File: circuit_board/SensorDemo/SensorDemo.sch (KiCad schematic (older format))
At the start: 47 parts, among them K1 PB, P1 CONN3X2, P2 CONN3X2, U1 TLV1117-33CDCYR, U2 dsPIC33EP32GP502, U3 LTC1658, U4 INA126, U5 REF1925, U6 REF1925, X1 CRYSTAL

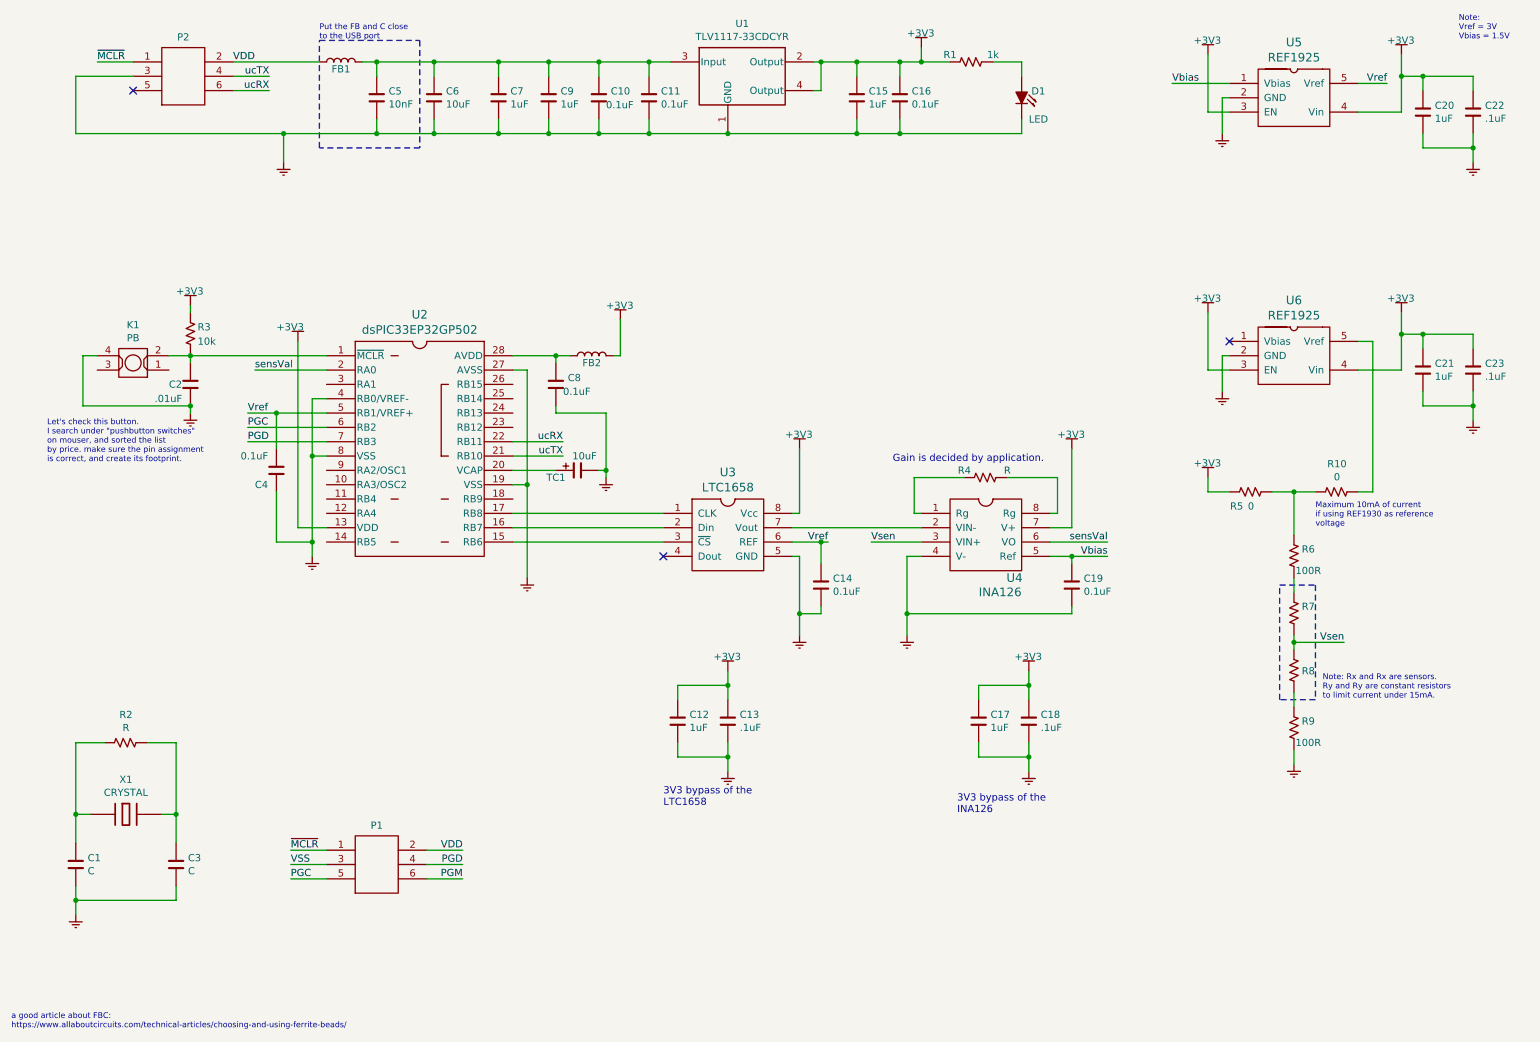
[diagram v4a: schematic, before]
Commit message: symbol and pcb footprint updated
Added test points to replace the sensors.
TC2030 part modified.
the button needs modification.
TG connector:
https://www.tag-connect.com/product/tc2030-alt-nl-no-legs-cable-for-use-with-altera-usb-blaster
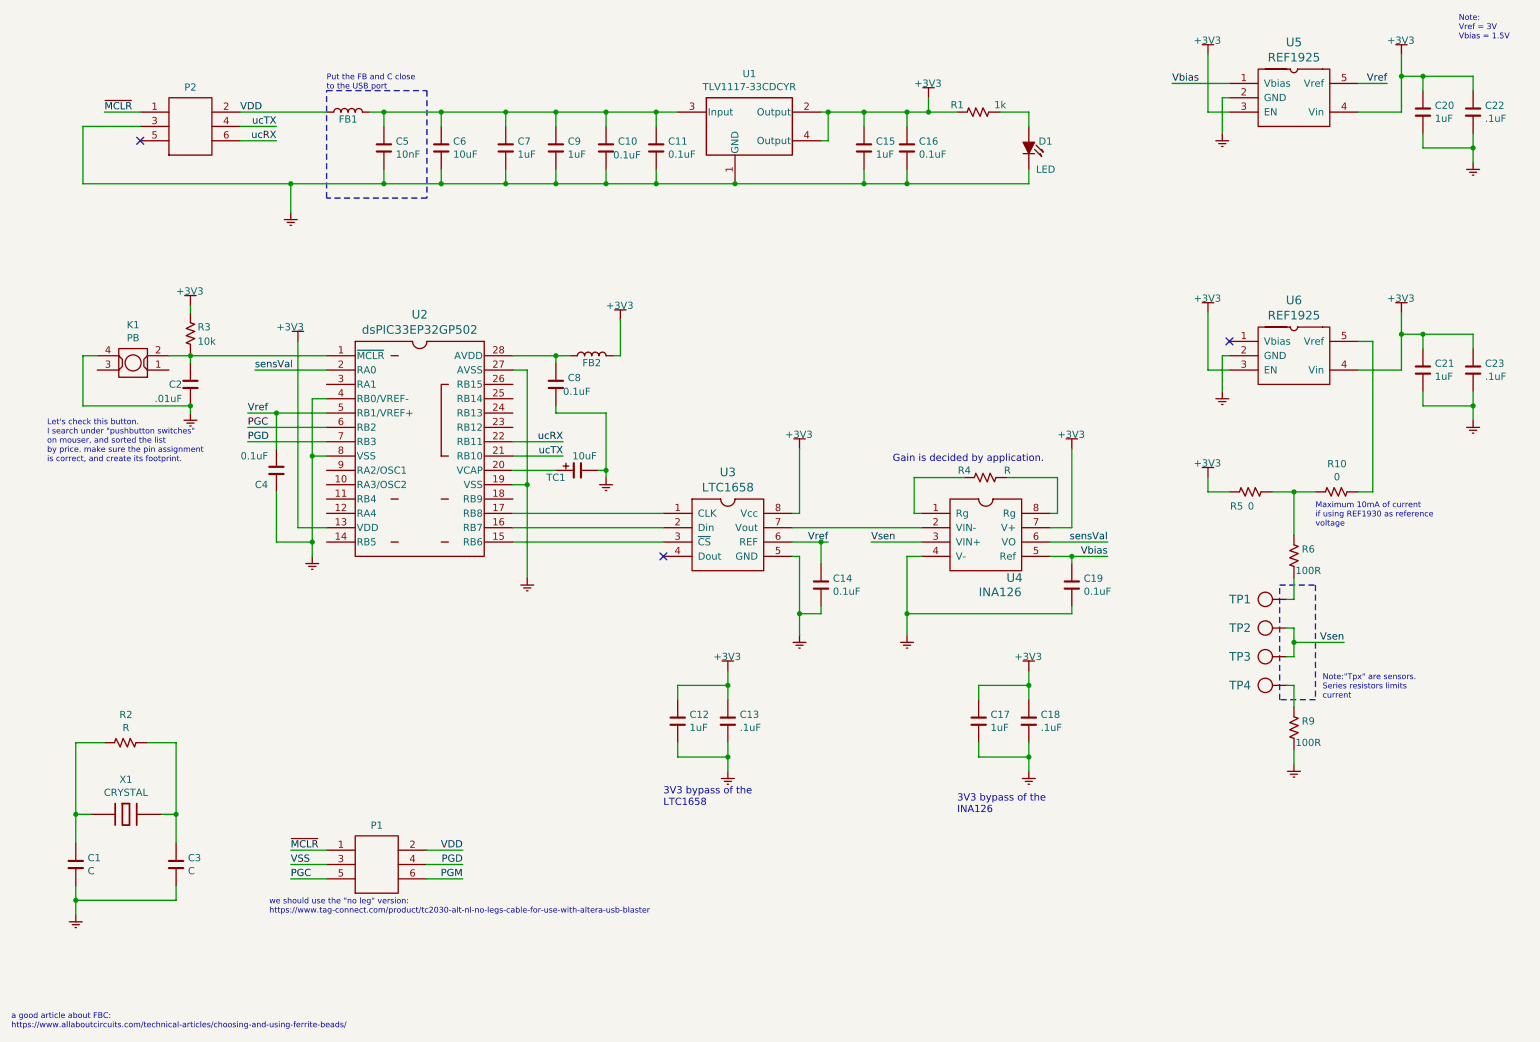
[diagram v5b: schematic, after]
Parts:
- removed R7, R8: R, symbol SensorDemo_passive:R
- added TP1, TP2, TP3, TP4: TP, SensorDemo_pcb:TP_SMD_2MM, symbol SensorDemo_discrete:TP
- FB1, FB2: footprint (none) -> SensorDemo_pcb:R0805
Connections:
- net Vsen: now also TP2.1, TP3.1
- net at R6.2: now also TP1.1
- net at R9.1: now also TP4.1
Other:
- note added: "Note:"Tpx" are sensors.\nSeries resistors limits\ncurrent"
- note added: "we should use the "no leg" version:\nhttps://www.tag-connect.com/product/tc2030-alt-nl-no-legs-cable-for-use-with-altera-usb-blaster"
- note removed: "Note: Rx and Rx are sensors.\nRy and Ry are constant resistors\nto limit current under 15mA."
- moved on the sheet: C10, C11, C15, C16, C5, C6, C7, C9, D1, FB1, P2, R1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

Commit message: updated schematic
-fixed footprints
-spread parts
-connected some traces
- found FB (1kOhm, 1A)
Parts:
- added MH1, MH2, MH3, MH4, MH5, MH6, MH7: MH, SensorDemo_pcb:MH_3MM, symbol SensorDemo_discrete:MH
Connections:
- net OSC1: now reaches U2.10 (RA3/OSC2)
- net OSC1: now also C1.1, R2.1, U2.9 (RA2/OSC1), X1.1
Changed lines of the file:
@@
 F 1 "12.3071 nano ohm" H 2975 1450 50  0001 C CNN
 F 2 "SensorDemo_pcb:R0805" H 2900 1350 50  0001 C CNN
-F 3 "" H 2900 1350 50  0001 C CNN
+F 3 "https://www.mouser.com/ProductDetail/Fair-Rite/2508051027Y1?qs=paL1wOLBYNd1w0Ok9jKq0w%3D%3D" H 2900 1350 50  0001 C CNN
 	1    2900 1350
 	1    0    0    -1
@@
 F 1 "12.3071 nano ohm" H 4675 3150 50  0001 C CNN
 F 2 "SensorDemo_pcb:R0805" H 4600 3050 50  0001 C CNN
-F 3 "" H 4600 3050 50  0001 C CNN
+F 3 "https://www.mouser.com/ProductDetail/Fair-Rite/2508051027Y1?qs=paL1wOLBYNd1w0Ok9jKq0w%3D%3D" H 4600 3050 50  0001 C CNN
 	1    4600 3050
 	1    0    0    -1
@@
 Wire Wire Line
 	9500 5350 9450 5350
+Wire Wire Line
+	1700 5450 1000 5450
+Wire Wire Line
+	1000 5450 1000 5750
+Connection ~ 1000 5750
+Wire Wire Line
+	1700 5200 1000 5200
+Wire Wire Line
+	1000 5200 1000 5450
+Connection ~ 1000 5450
+Wire Wire Line
+	2100 4100 2600 4100
+Wire Wire Line
+	2600 4100 2600 3850
+Wire Wire Line
+	2600 3850 2750 3850
+Wire Wire Line
+	2100 4200 2700 4200
+Wire Wire Line
+	2700 4200 2700 3950
+Wire Wire Line
+	2700 3950 2750 3950
+Text Label 2100 4100 0    50   ~ 0
+OSC1
+Text Label 2100 4200 0    50   ~ 0
+OSC2
+Text Label 1700 5200 2    50   ~ 0
+OSC1
+Text Label 1700 5450 2    50   ~ 0
+OSC2
+$Comp
+L SensorDemo_discrete:MH MH1
+U 1 1 6041AA27
+P 2650 5300
+F 0 "MH1" H 2778 5300 60  0000 L CNN
+F 1 "MH" H 2650 5300 60  0001 C CNN
+F 2 "SensorDemo_pcb:MH_3MM" H 2650 5300 60  0001 C CNN
+F 3 "" H 2650 5300 60  0000 C CNN
+	1    2650 5300
+	1    0    0    -1
+$EndComp
+$Comp
+L SensorDemo_discrete:MH MH3
+U 1 1 6041B104
+P 3100 5300
+F 0 "MH3" H 3228 5300 60  0000 L CNN
+F 1 "MH" H 3100 5300 60  0001 C CNN
+F 2 "SensorDemo_pcb:MH_3MM" H 3100 5300 60  0001 C CNN
+F 3 "" H 3100 5300 60  0000 C CNN
+	1    3100 5300
+	1    0    0    -1
+$EndComp
+$Comp
+L SensorDemo_discrete:MH MH5
+U 1 1 6041B3CD
+P 3550 5300
+F 0 "MH5" H 3678 5300 60  0000 L CNN
+F 1 "MH" H 3550 5300 60  0001 C CNN
+F 2 "SensorDemo_pcb:MH_3MM" H 3550 5300 60  0001 C CNN
+F 3 "" H 3550 5300 60  0000 C CNN
+	1    3550 5300
+	1    0    0    -1
+$EndComp
+$Comp
+L SensorDemo_discrete:MH MH7
+U 1 1 6041B6C9
+P 4000 5300
+F 0 "MH7" H 4128 5300 60  0000 L CNN
+F 1 "MH" H 4000 5300 60  0001 C CNN
+F 2 "SensorDemo_pcb:MH_3MM" H 4000 5300 60  0001 C CNN
+F 3 "" H 4000 5300 60  0000 C CNN
+	1    4000 5300
+	1    0    0    -1
+$EndComp
+$Comp
+L SensorDemo_discrete:MH MH2
+U 1 1 6041C7FF
+P 2900 5600
+F 0 "MH2" H 3028 5600 60  0000 L CNN
+F 1 "MH" H 2900 5600 60  0001 C CNN
+F 2 "SensorDemo_pcb:MH_3MM" H 2900 5600 60  0001 C CNN
+F 3 "" H 2900 5600 60  0000 C CNN
+	1    2900 5600
+	1    0    0    -1
+$EndComp
+$Comp
+L SensorDemo_discrete:MH MH4
+U 1 1 6041CC94
+P 3350 5600
+F 0 "MH4" H 3478 5600 60  0000 L CNN
+F 1 "MH" H 3350 5600 60  0001 C CNN
+F 2 "SensorDemo_pcb:MH_3MM" H 3350 5600 60  0001 C CNN
+F 3 "" H 3350 5600 60  0000 C CNN
+	1    3350 5600
+	1    0    0    -1
+$EndComp
+$Comp
+L SensorDemo_discrete:MH MH6
+U 1 1 6041D148
+P 3800 5600
+F 0 "MH6" H 3928 5600 60  0000 L CNN
+F 1 "MH" H 3800 5600 60  0001 C CNN
+F 2 "SensorDemo_pcb:MH_3MM" H 3800 5600 60  0001 C CNN
+F 3 "" H 3800 5600 60  0000 C CNN
+	1    3800 5600
+	1    0    0    -1
+$EndComp
 $EndSCHEMATC

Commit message: PCB edited
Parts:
- added C24: 1uF, SensorDemo_pcb:C0805, symbol SensorDemo_passive:C
- added C25: .1uF, SensorDemo_pcb:C0805, symbol SensorDemo_passive:C
- C1, C3: value C -> 22pF
- R10, R5: value 0 -> 0R
- R2: value R -> 1M
- X1: value CRYSTAL -> 8MHz
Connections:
- net OSC1: no longer U2.10 (RA3/OSC2)
- net VDD: no longer FB1.1, P2.2
- net ucRX: now also P2.4; no longer P2.6
- net ucTX: now also P2.2; no longer P2.4
- net ~MCLR: no longer P2.1
- net at C10.2, C11.2, C15.2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: now also P2.1
- net at P2.5: now also FB1.1, P2.6
- net OSC2: now reaches C3.1, R2.2, X1.2
- net OSC2: now also U2.10 (RA3/OSC2)
- new net: C24.1, C25.1
- new net: C24.2, C25.2
- no-connect marks 3 -> 2
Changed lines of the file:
@@
 Vref
-Wire Wire Line
-	6250 4350 6200 4350
 Wire Wire Line
 	4050 4350 5100 4350
@@
 Wire Wire Line
 	6900 4250 6000 4250
-$Comp
-L SensorDemo_power_supply:GND #PS0107
-U 1 1 60286B29
-P 6050 5050
-F 0 "#PS0107" H 6050 4925 50  0001 C CNN
-F 1 "GND" H 6050 4975 50  0001 C CNN
-F 2 "" H 6050 5050 50  0001 C CNN
-F 3 "" H 6050 5050 50  0001 C CNN
-	1    6050 5050
-	1    0    0    -1
-$EndComp
 Wire Wire Line
 	6050 4450 6000 4450
-Wire Wire Line
-	6050 5000 6050 4850
 $Comp
 L SensorDemo_IC:LTC1658 U3
@@
 Connection ~ 4700 3850
 NoConn ~ 9050 2950
-$Comp
-L SensorDemo_passive:C C14
-U 1 1 6037670C
-P 6200 4650
-F 0 "C14" V 6154 4733 50  0000 L CNN
-F 1 "0.1uF" V 6245 4733 50  0000 L CNN
-F 2 "SensorDemo_pcb:C0805" H 6238 4500 30  0001 C CNN
-F 3 "" H 6200 4650 60  0000 C CNN
-	1    6200 4650
-	0    1    1    0
-$EndComp
-Wire Wire Line
-	6200 4500 6200 4350
-Connection ~ 6200 4350
-Wire Wire Line
-	6200 4350 6000 4350
-Wire Wire Line
-	6200 4800 6200 4850
-Wire Wire Line
-	6200 4850 6050 4850
-Connection ~ 6050 4850
-Wire Wire Line
-	6050 4850 6050 4450
 Text Notes 6700 3800 0    50   ~ 0
 Gain is decided by application.
@@
 F 3 "https://www.tag-connect.com/product/tc2030-alt-nl-no-legs-cable-for-use-with-altera-usb-blaster" H 5100 -700 60  0001 C CNN
 	1    1800 1450
-	1    0    0    -1
-$EndComp
-Wire Wire Line
-	1200 1350 1450 1350
-Wire Wire Line
-	2150 1350 2750 1350
-Text Label 2300 1350 2    50   ~ 0
-VDD
-Text Label 1200 1350 0    50   ~ 0
-~MCLR
-Wire Wire Line
-	1050 1450 1050 1850
-Wire Wire Line
-	1050 1850 2500 1850
-Wire Wire Line
-	1050 1450 1450 1450
+	1    0    0    1
+$EndComp
+Wire Wire Line
+	2150 1350 2300 1350
+Wire Wire Line
+	1350 1850 2500 1850
 Wire Wire Line
 	2400 1450 2150 1450
+Text Label 2400 1550 2    50   ~ 0
+ucTX
+Wire Wire Line
+	2400 1550 2150 1550
 Text Label 2400 1450 2    50   ~ 0
-ucTX
-Wire Wire Line
-	2400 1550 2150 1550
-Text Label 2400 1550 2    50   ~ 0
 ucRX
 $Comp
@@
 U 1 1 60353991
 P 1350 5750
-F 0 "R2" H 1350 5945 50  0000 C CNN
-F 1 "R" H 1350 5854 50  0000 C CNN
+F 0 "R2" H 1200 5700 50  0000 C CNN
+F 1 "1M" H 1500 5700 50  0000 C CNN
 F 2 "SensorDemo_pcb:R0805" H 1300 5680 30  0001 C CNN
 F 3 "" V 1350 5750 30  0001 C CNN
@@
 P 1000 6600
 F 0 "C1" V 954 6683 50  0000 L CNN
-F 1 "C" V 1045 6683 50  0000 L CNN
+F 1 "22pF" V 1045 6683 50  0000 L CNN
 F 2 "SensorDemo_pcb:C0805" H 1038 6450 30  0001 C CNN
-F 3 "" H 1000 6600 60  0000 C CNN
+F 3 "" H 1000 6600 60  0001 C CNN
 	1    1000 6600
 	0    1    1    0
@@
 P 1700 6600
 F 0 "C3" V 1654 6683 50  0000 L CNN
-F 1 "C" V 1745 6683 50  0000 L CNN
+F 1 "22pF" V 1745 6683 50  0000 L CNN
 F 2 "SensorDemo_pcb:C0805" H 1738 6450 30  0001 C CNN
-F 3 "" H 1700 6600 60  0000 C CNN
+F 3 "" H 1700 6600 60  0001 C CNN
 	1    1700 6600
 	0    1    1    0
@@
 P 1350 6250
 F 0 "X1" H 1350 6493 50  0000 C CNN
-F 1 "CRYSTAL" H 1350 6402 50  0000 C CNN
+F 1 "8MHz" H 1350 6402 50  0000 C CNN
 F 2 "SensorDemo_pcb:CRYSTAL_ABM3-8.000MHz-D2Y-T" H 1350 6250 60  0001 C CNN
 F 3 "https://www.mouser.com/ProductDetail/ABRACON/ABM3-8000MHZ-B4Y-T?qs=%252BlF%252B75lapNKxd1hbTYfShQ%3D%3D" H 1350 6409 60  0001 C CNN
@@
 Text Notes 800  3800 0    40   ~ 0
 Let's check this button. \nI search under "pushbutton switches"\non mouser, and sorted the list\nby price. make sure the pin assignment\nis correct, and create its footprint.
-NoConn ~ 1450 1550
 Text Label 3700 6700 2    50   ~ 0
 PGM
@@
 P 9800 4000
 F 0 "R10" H 9800 4195 50  0000 C CNN
-F 1 "0" H 9800 4104 50  0000 C CNN
+F 1 "0R" H 9800 4104 50  0000 C CNN
 F 2 "SensorDemo_pcb:R0805" H 9750 3930 30  0001 C CNN
 F 3 "" V 9800 4000 30  0001 C CNN
@@
 U 1 1 6040CF70
 P 9200 4000
-F 0 "R5" H 9100 3900 50  0000 C CNN
-F 1 "0" H 9200 3900 50  0000 C CNN
+F 0 "R5" H 9200 4100 50  0000 C CNN
+F 1 "0R" H 9200 3900 50  0000 C CNN
 F 2 "SensorDemo_pcb:R0805" H 9150 3930 30  0001 C CNN
 F 3 "" V 9200 4000 30  0001 C CNN
@@
 	9500 5350 9450 5350
 Wire Wire Line
-	1700 5450 1000 5450
-Wire Wire Line
-	1000 5450 1000 5750
+	1950 5750 1700 5750
 Connection ~ 1000 5750
 Wire Wire Line
-	1700 5200 1000 5200
-Wire Wire Line
-	1000 5200 1000 5450
-Connection ~ 1000 5450
+	1950 5550 1000 5550
 Wire Wire Line
 	2100 4100 2600 4100
@@
 Text Label 2100 4100 0    50   ~ 0
 OSC1
-Text Label 2100 4200 0    50   ~ 0
-OSC2
-Text Label 1700 5200 2    50   ~ 0
+Text Label 1950 5550 2    50   ~ 0
 OSC1
-Text Label 1700 5450 2    50   ~ 0
+Text Label 1950 5750 2    50   ~ 0
 OSC2
 $Comp
@@
 	1    0    0    -1
 $EndComp
+Text Label 2100 4200 0    50   ~ 0
+OSC2
+Connection ~ 1700 5750
+Wire Wire Line
+	1000 5550 1000 5750
+$Comp
+L SensorDemo_passive:C C24
+U 1 1 60489E51
+P 1350 4500
+F 0 "C24" V 1304 4583 50  0000 L CNN
+F 1 "1uF" V 1395 4583 50  0000 L CNN
+F 2 "SensorDemo_pcb:C0805" H 1388 4350 30  0001 C CNN
+F 3 "" H 1350 4500 60  0000 C CNN
+	1    1350 4500
+	0    1    1    0
+$EndComp
+$Comp
+L SensorDemo_passive:C C25
+U 1 1 60489E5B
+P 1700 4500
+F 0 "C25" V 1654 4583 50  0000 L CNN
+F 1 ".1uF" V 1745 4583 50  0000 L CNN
+F 2 "SensorDemo_pcb:C0805" H 1738 4350 30  0001 C CNN
+F 3 "" H 1700 4500 60  0000 C CNN
+	1    1700 4500
+	0    1    1    0
+$EndComp
+Wire Wire Line
+	1350 4350 1350 4250
+Wire Wire Line
+	1700 4350 1700 4250
+Wire Wire Line
+	1700 4250 1350 4250
+Wire Wire Line
+	1350 4650 1350 4750
+Wire Wire Line
+	1350 4750 1700 4750
+Wire Wire Line
+	1700 4750 1700 4650
+$Comp
+L SensorDemo_power_supply:GND #PS0124
+U 1 1 60489E6B
+P 1700 4900
+F 0 "#PS0124" H 1700 4775 50  0001 C CNN
+F 1 "GND" H 1700 4825 50  0001 C CNN
+F 2 "" H 1700 4900 50  0001 C CNN
+F 3 "" H 1700 4900 50  0001 C CNN
+	1    1700 4900
+	1    0    0    -1
+$EndComp
+Wire Wire Line
+	1700 4750 1700 4850
+Connection ~ 1700 4750
+$Comp
+L SensorDemo_power_supply:+3V3 #PS0125
+U 1 1 60489E77
+P 1700 4150
+F 0 "#PS0125" H 1700 4100 50  0001 C CNN
+F 1 "+3V3" H 1600 4250 50  0000 L CNN
+F 2 "" H 1705 3845 50  0001 C CNN
+F 3 "" H 1705 3845 50  0001 C CNN
+	1    1700 4150
+	1    0    0    -1
+$EndComp
+Wire Wire Line
+	1700 4150 1700 4250
+Connection ~ 1700 4250
+$Comp
+L SensorDemo_power_supply:GND #PS0107
+U 1 1 60286B29
+P 6050 5050
+F 0 "#PS0107" H 6050 4925 50  0001 C CNN
+F 1 "GND" H 6050 4975 50  0001 C CNN
+F 2 "" H 6050 5050 50  0001 C CNN
+F 3 "" H 6050 5050 50  0001 C CNN
+	1    6050 5050
+	1    0    0    -1
+$EndComp
+Wire Wire Line
+	6050 4850 6050 4450
+Wire Wire Line
+	6050 5000 6050 4850
+Connection ~ 6050 4850
+Wire Wire Line
+	6200 4850 6050 4850
+Wire Wire Line
+	6200 4800 6200 4850
+Wire Wire Line
+	6200 4350 6000 4350
+Wire Wire Line
+	6250 4350 6200 4350
+Connection ~ 6200 4350
+Wire Wire Line
+	6200 4500 6200 4350
+$Comp
+L SensorDemo_passive:C C14
+U 1 1 6037670C
+P 6200 4650
+F 0 "C14" V 6154 4733 50  0000 L CNN
+F 1 "0.1uF" V 6245 4733 50  0000 L CNN
+F 2 "SensorDemo_pcb:C0805" H 6238 4500 30  0001 C CNN
+F 3 "" H 6200 4650 60  0000 C CNN
+	1    6200 4650
+	0    1    1    0
+$EndComp
+Wire Wire Line
+	1450 1550 1350 1550
+Wire Wire Line
+	1350 1550 1350 1850
+Wire Wire Line
+	1350 1550 1350 1450
+Wire Wire Line
+	1350 1450 1450 1450
+Connection ~ 1350 1550
+Wire Wire Line
+	1450 1350 1350 1350
+Wire Wire Line
+	1350 1350 1350 1150
+Wire Wire Line
+	1350 1150 2300 1150
+Wire Wire Line
+	2300 1150 2300 1350
+Connection ~ 2300 1350
+Wire Wire Line
+	2300 1350 2750 1350
 $EndSCHEMATC
